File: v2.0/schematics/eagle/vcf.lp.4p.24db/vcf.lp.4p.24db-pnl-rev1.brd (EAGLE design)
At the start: 30 x 128 mm, 0 parts

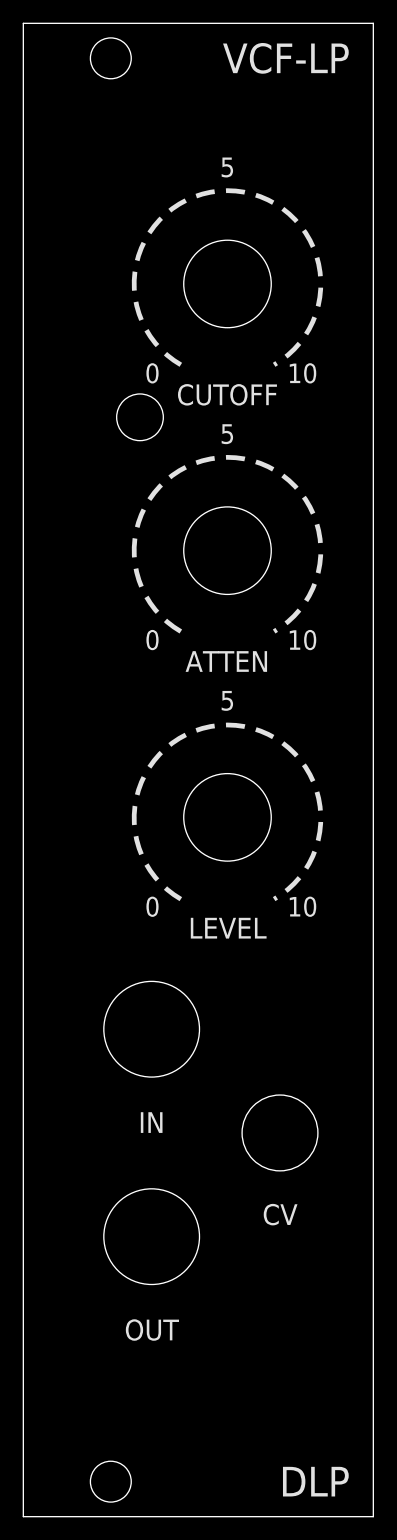
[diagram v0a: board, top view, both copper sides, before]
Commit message: VCF-LF: Schem cleanup for removed ICs; update panel
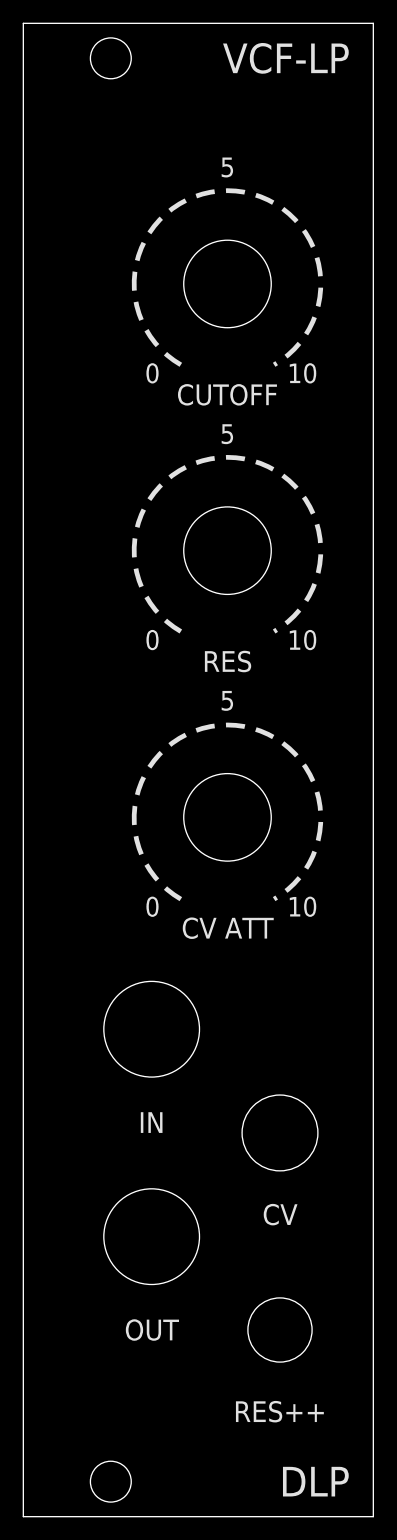
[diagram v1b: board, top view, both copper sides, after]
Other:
- board text added: "CV ATT"
- board text added: "RES"
- board text added: "RES++"
- board text removed: "ATTEN"
- board text removed: "LEVEL"
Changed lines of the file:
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@@
 <hole x="17.5" y="105.66" drill="7.5" grouprefs="POTS"/>
 <hole x="22" y="32.89" drill="6.5"/>
-<hole x="10" y="94.23" drill="4"/>
+<hole x="22" y="16" drill="5.5"/>
 <hole x="7.5" y="125" drill="3.5"/>
 <hole x="7.5" y="3" drill="3.5"/>
 <text x="17.5" y="96.16" size="1.778" layer="25" align="center">CUTOFF</text>
-<text x="17.5" y="73.3" size="1.778" layer="25" align="center">ATTEN</text>
-<text x="17.5" y="50.44" size="1.778" layer="25" align="center">LEVEL</text>
+<text x="17.5" y="73.3" size="1.778" layer="25" align="center">RES</text>
+<text x="17.5" y="50.44" size="1.778" layer="25" align="center">CV ATT</text>
 <text x="11" y="33.78" size="1.778" layer="25" align="center">IN</text>
 <text x="11" y="16" size="1.778" layer="25" align="center">OUT</text>
@@
 <text x="17.5" y="69.94" size="1.6764" layer="25" align="center">5</text>
 <text x="11.072" y="52.28" size="1.6764" layer="25" align="center">0</text>
+<text x="22" y="9" size="1.778" layer="25" align="center">RES++</text>
 </plain>
 <attributes>

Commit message: Panel revisions; VCF-LP board layout
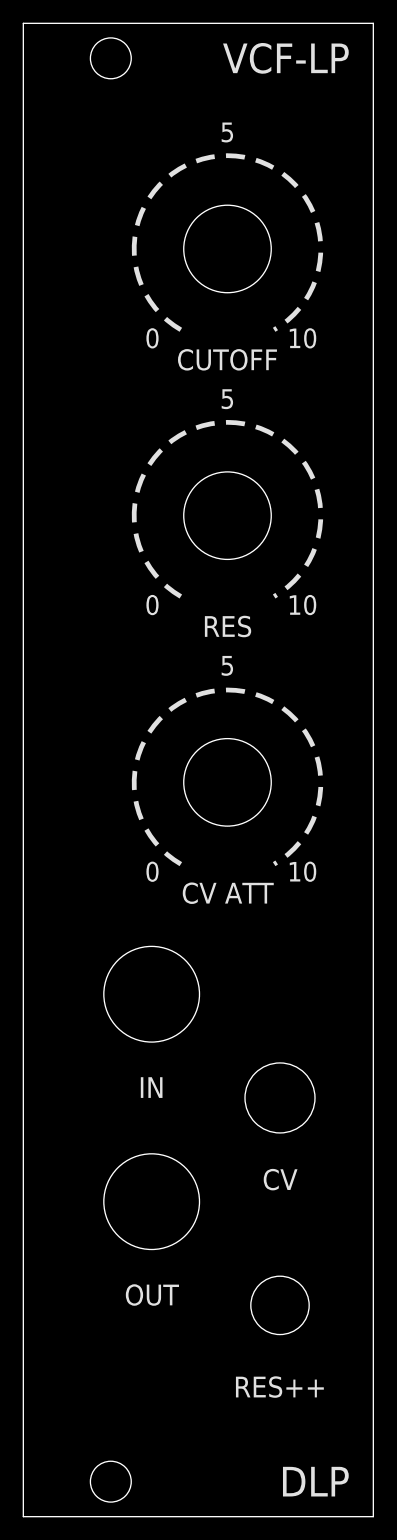
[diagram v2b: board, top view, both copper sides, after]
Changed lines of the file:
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@@
 <wire x1="30" y1="128" x2="0" y2="128" width="0" layer="20"/>
 <wire x1="0" y1="128" x2="0" y2="0" width="0" layer="20"/>
-<hole x="17.5" y="82.8" drill="7.5" grouprefs="POTS"/>
-<hole x="11" y="41.78" drill="8.2" grouprefs="JACKS"/>
-<hole x="11" y="24" drill="8.2" grouprefs="JACKS"/>
-<hole x="17.5" y="59.94" drill="7.5" grouprefs="POTS"/>
-<hole x="17.5" y="105.66" drill="7.5" grouprefs="POTS"/>
-<hole x="22" y="32.89" drill="6.5"/>
-<hole x="22" y="16" drill="5.5"/>
+<hole x="17.5" y="85.8" drill="7.5" grouprefs="POTS"/>
+<hole x="11" y="44.78" drill="8.2" grouprefs="JACKS"/>
+<hole x="11" y="27" drill="8.2" grouprefs="JACKS"/>
+<hole x="17.5" y="62.94" drill="7.5" grouprefs="POTS"/>
+<hole x="17.5" y="108.66" drill="7.5" grouprefs="POTS"/>
+<hole x="22" y="35.89" drill="6"/>
+<hole x="22" y="18.11" drill="5"/>
 <hole x="7.5" y="125" drill="3.5"/>
 <hole x="7.5" y="3" drill="3.5"/>
-<text x="17.5" y="96.16" size="1.778" layer="25" align="center">CUTOFF</text>
-<text x="17.5" y="73.3" size="1.778" layer="25" align="center">RES</text>
-<text x="17.5" y="50.44" size="1.778" layer="25" align="center">CV ATT</text>
-<text x="11" y="33.78" size="1.778" layer="25" align="center">IN</text>
-<text x="11" y="16" size="1.778" layer="25" align="center">OUT</text>
-<text x="22" y="25.89" size="1.778" layer="25" align="center">CV</text>
+<text x="17.5" y="99.16" size="1.778" layer="25" align="center">CUTOFF</text>
+<text x="17.5" y="76.3" size="1.778" layer="25" align="center">RES</text>
+<text x="17.5" y="53.44" size="1.778" layer="25" align="center">CV ATT</text>
+<text x="11" y="36.78" size="1.778" layer="25" align="center">IN</text>
+<text x="11" y="19" size="1.778" layer="25" align="center">OUT</text>
+<text x="22" y="28.89" size="1.778" layer="25" align="center">CV</text>
 <text x="28" y="3" size="2.54" layer="25" align="center-right">DLP</text>
 <text x="28" y="125" size="2.54" layer="25" align="center-right">VCF-LP</text>
-<wire x1="13.5" y1="98.73" x2="21.5" y2="98.73" width="0.4064" layer="25" style="shortdash" curve="-300"/>
-<wire x1="13.5" y1="75.87" x2="21.5" y2="75.87" width="0.4064" layer="25" style="shortdash" curve="-300"/>
-<wire x1="13.5" y1="52.93" x2="21.5" y2="52.93" width="0.4064" layer="25" style="shortdash" curve="-300"/>
-<text x="11.072" y="98" size="1.6764" layer="25" align="center">0</text>
-<text x="23.928" y="98" size="1.6764" layer="25" align="center">10</text>
-<text x="17.5" y="115.66" size="1.6764" layer="25" align="center">5</text>
-<text x="11.072" y="75.14" size="1.6764" layer="25" align="center">0</text>
-<text x="17.5" y="92.8" size="1.6764" layer="25" align="center">5</text>
-<text x="23.928" y="75.14" size="1.6764" layer="25" align="center">10</text>
-<text x="23.928" y="52.28" size="1.6764" layer="25" align="center">10</text>
-<text x="17.5" y="69.94" size="1.6764" layer="25" align="center">5</text>
-<text x="11.072" y="52.28" size="1.6764" layer="25" align="center">0</text>
-<text x="22" y="9" size="1.778" layer="25" align="center">RES++</text>
+<wire x1="13.5" y1="101.73" x2="21.5" y2="101.73" width="0.4064" layer="25" style="shortdash" curve="-300"/>
+<wire x1="13.5" y1="78.87" x2="21.5" y2="78.87" width="0.4064" layer="25" style="shortdash" curve="-300"/>
+<wire x1="13.5" y1="55.93" x2="21.5" y2="55.93" width="0.4064" layer="25" style="shortdash" curve="-300"/>
+<text x="11.072" y="101" size="1.6764" layer="25" align="center">0</text>
+<text x="23.928" y="101" size="1.6764" layer="25" align="center">10</text>
+<text x="17.5" y="118.66" size="1.6764" layer="25" align="center">5</text>
+<text x="11.072" y="78.14" size="1.6764" layer="25" align="center">0</text>
+<text x="17.5" y="95.8" size="1.6764" layer="25" align="center">5</text>
+<text x="23.928" y="78.14" size="1.6764" layer="25" align="center">10</text>
+<text x="23.928" y="55.28" size="1.6764" layer="25" align="center">10</text>
+<text x="17.5" y="72.94" size="1.6764" layer="25" align="center">5</text>
+<text x="11.072" y="55.28" size="1.6764" layer="25" align="center">0</text>
+<text x="22" y="11.11" size="1.778" layer="25" align="center">RES++</text>
 </plain>
 <attributes>
